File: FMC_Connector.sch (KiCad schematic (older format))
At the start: 1 part, among them J1 ASP-134488-01

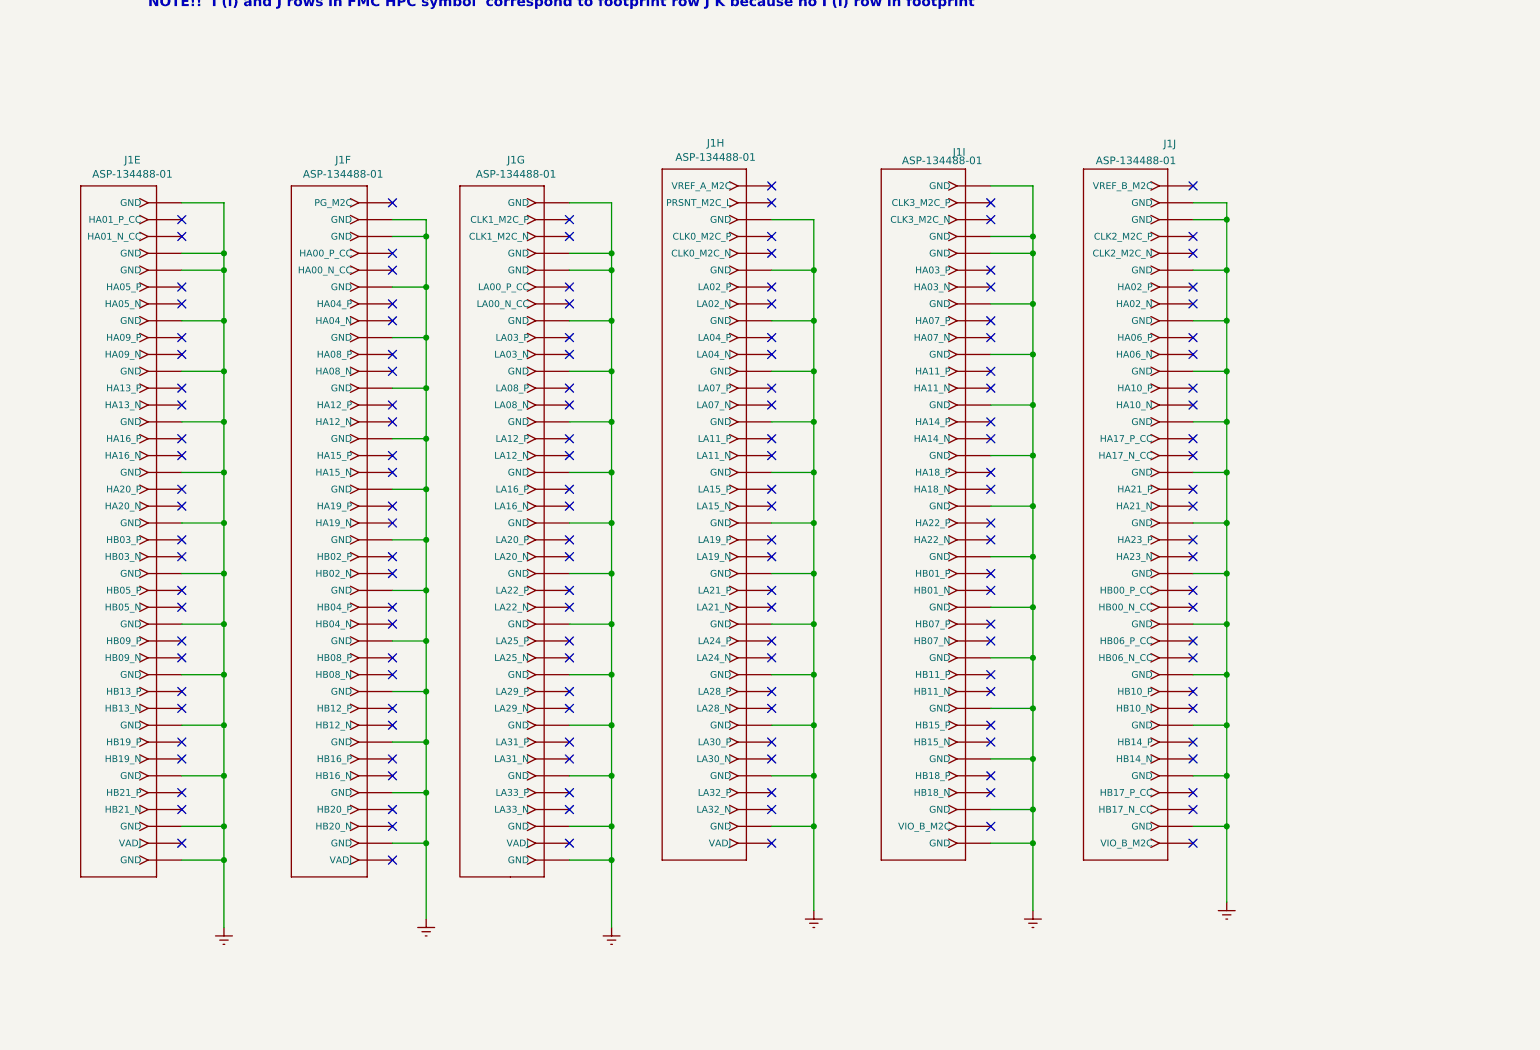
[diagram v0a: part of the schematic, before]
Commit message: adding more power supplies
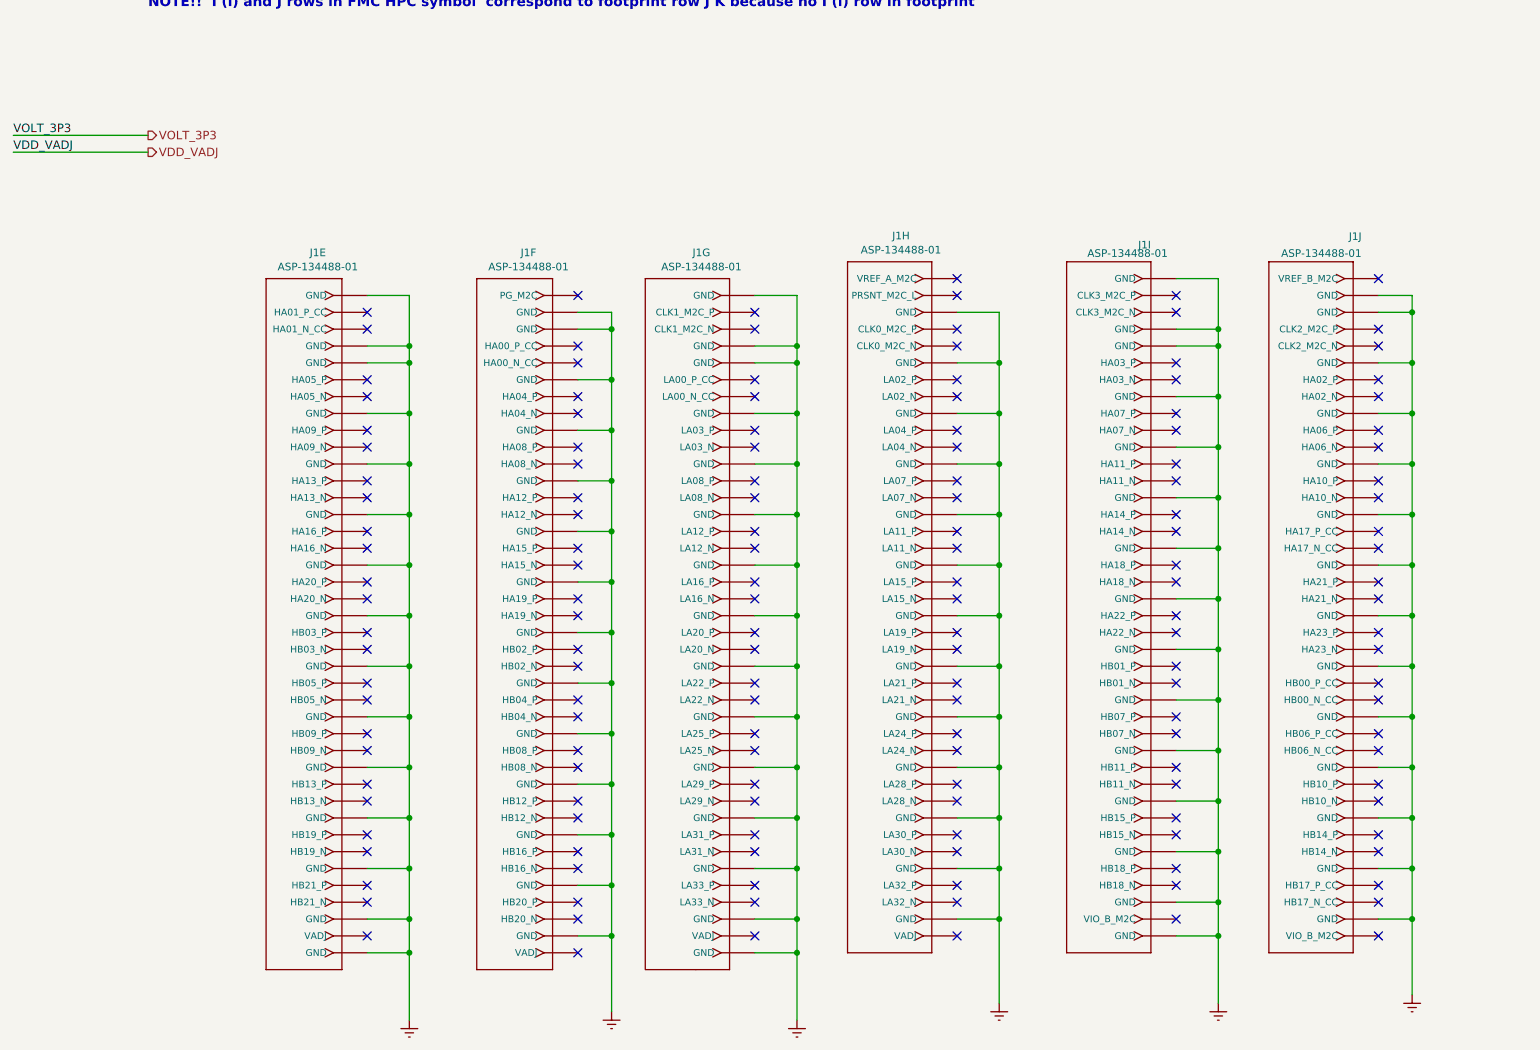
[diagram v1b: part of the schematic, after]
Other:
- moved on the sheet: J1E, J1F, J1G, J1H, J1I, J1J

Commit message: populating FMC connector
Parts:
- added R18: 0, Resistors_SMD:R_0805, symbol Device:R
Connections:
- net VDD_VADJ: now also J1.E39 (VADJ), J1.F40 (VADJ), J1.G39 (VADJ), J1.H40 (VADJ)
- net VOLT_3P3: now also J1.C39 (3PV3), J1.D36 (3P3V), J1.D38 (3P3V), J1.D40 (3P3V)
- net TDI: now reaches J1.D30 (TDI)
- net TDI: now also R18.1
- net TDO: now reaches J1.D31 (TDO)
- net TDO: now also R18.2
- no-connect marks 314 -> 304
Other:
- moved on the sheet: J1A, J1B, J1C, J1D, J1E, J1F, J1G, J1H, J1I, J1J
